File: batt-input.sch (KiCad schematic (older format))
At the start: 50 parts

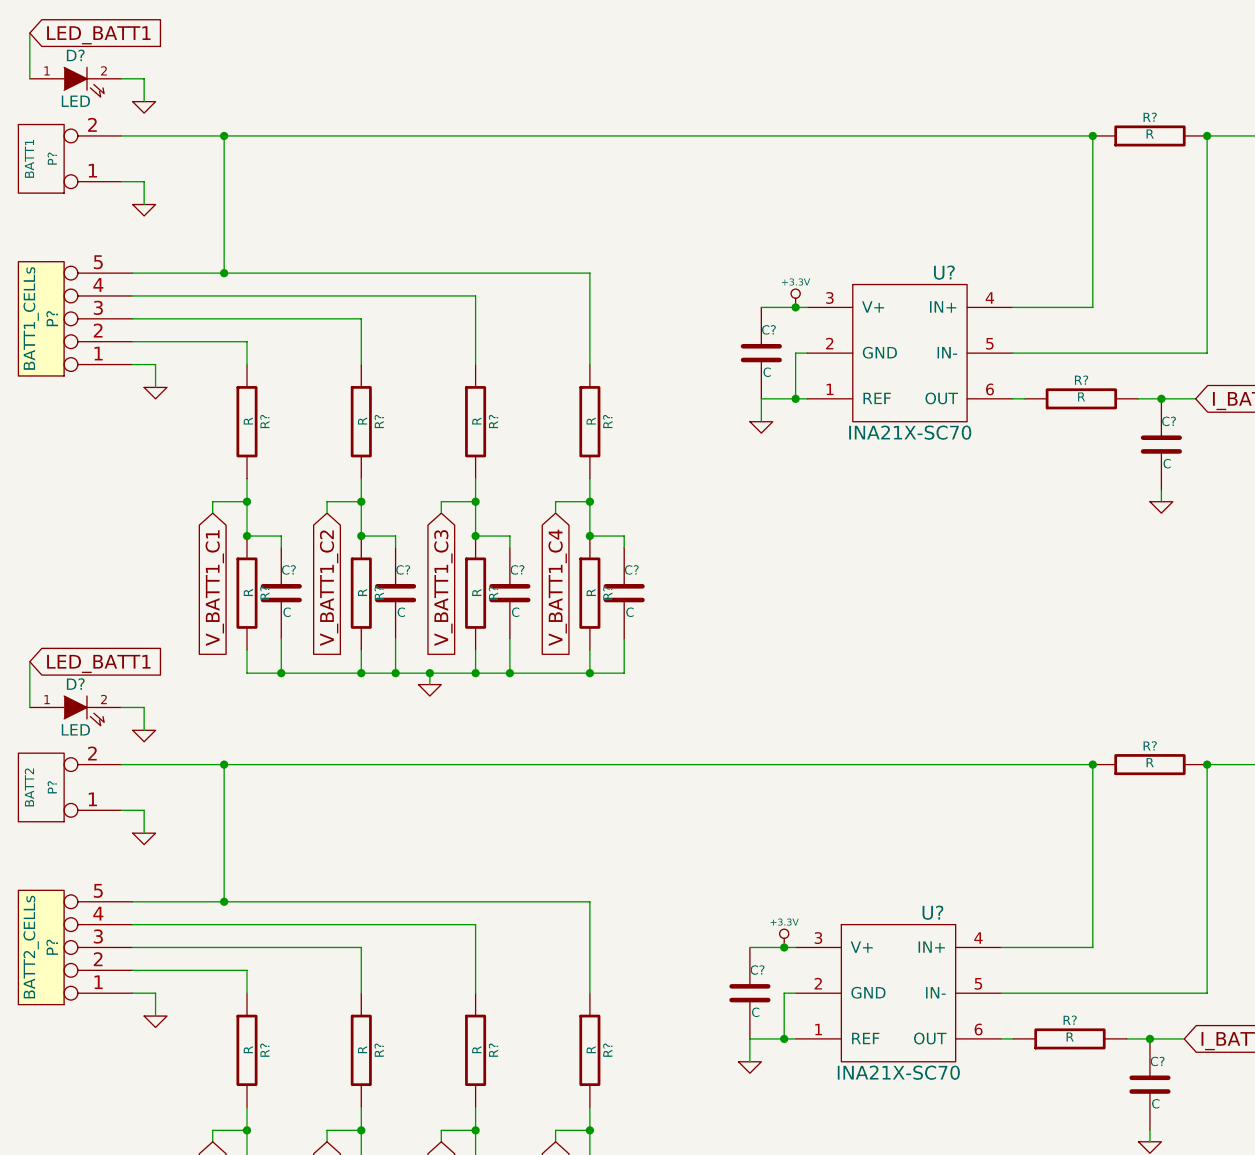
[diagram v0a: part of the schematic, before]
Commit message: Fuse on battery input
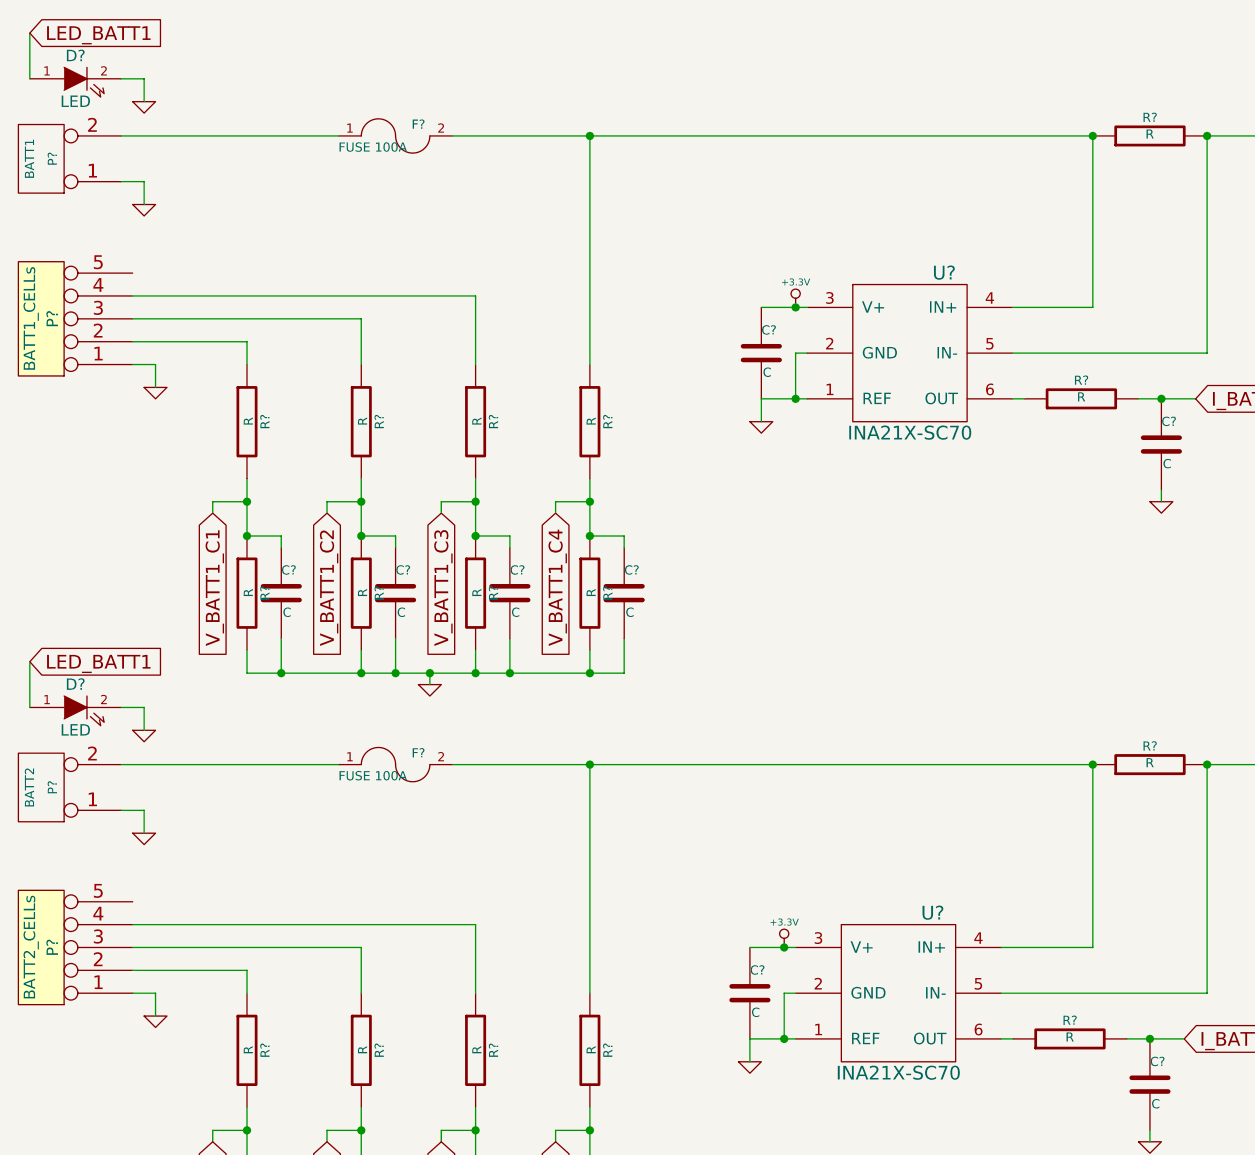
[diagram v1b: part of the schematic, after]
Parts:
- added F? (x2): FUSE 100A, ~, symbol FUSE
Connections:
- net at R?.1, R?.1, U?.4 (IN+): now also F?.2; no longer P?.2 (PM), P?.5 (x2)
- new net: F?.1, P?.2 (PM) (x2)
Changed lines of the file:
@@
 Sheet 2 5
 Title ""
-Date "28 dec 2014"
+Date "11 jan 2015"
 Rev ""
 Comp ""
@@
 	-1   0    0    1
 $EndComp
-Wire Wire Line
-	1100 2300 3100 2300
-Wire Wire Line
-	1500 2300 1500 1700
-Connection ~ 1500 1700
+Connection ~ 3100 1700
 $Comp
 L GND #PWR?
@@
 Wire Wire Line
 	1200 2700 1200 2800
-Connection ~ 1500 4450
+Connection ~ 3100 4450
 $Comp
 L GND #PWR?
@@
 Wire Wire Line
 	2600 2400 2600 2700
-Wire Wire Line
-	3100 2300 3100 2700
-Connection ~ 1500 2300
 Wire Wire Line
 	1600 3200 1600 3450
@@
 	4900 5250 5300 5250
 Wire Wire Line
-	5300 5250 5300 4450
+	5300 4450 5300 5250
 Connection ~ 5300 4450
 Connection ~ 5800 4450
@@
 Connection ~ 1750 4050
 Wire Wire Line
-	5300 4450 1050 4450
-Wire Wire Line
-	5300 1700 1050 1700
-Wire Wire Line
-	1100 5050 3100 5050
-Wire Wire Line
-	1500 5050 1500 4450
+	5300 1700 2500 1700
 $Comp
 L R R?
@@
 Wire Wire Line
 	2600 5150 2600 5450
-Wire Wire Line
-	3100 5050 3100 5450
-Connection ~ 1500 5050
 Wire Wire Line
 	1600 5950 1600 6200
@@
 Text HLabel 10700 3100 2    60   Output ~ 0
 PWR_OUT
+$Comp
+L FUSE F?
+U 1 1 54B23998
+P 2250 1700
+F 0 "F?" H 2350 1750 40  0000 C CNN
+F 1 "FUSE 100A" H 2150 1650 40  0000 C CNN
+F 2 "~" H 2250 1700 60  0000 C CNN
+F 3 "~" H 2250 1700 60  0000 C CNN
+	1    2250 1700
+	1    0    0    -1
+$EndComp
+Wire Wire Line
+	1050 1700 2000 1700
+Wire Wire Line
+	3100 2700 3100 1700
+Wire Wire Line
+	3100 5450 3100 4450
+$Comp
+L FUSE F?
+U 1 1 54B23E5C
+P 2250 4450
+F 0 "F?" H 2350 4500 40  0000 C CNN
+F 1 "FUSE 100A" H 2150 4400 40  0000 C CNN
+F 2 "~" H 2250 4450 60  0000 C CNN
+F 3 "~" H 2250 4450 60  0000 C CNN
+	1    2250 4450
+	1    0    0    -1
+$EndComp
+Wire Wire Line
+	1050 4450 2000 4450
+Wire Wire Line
+	2500 4450 5300 4450
 $EndSCHEMATC
